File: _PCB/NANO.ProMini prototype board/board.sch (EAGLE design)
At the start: 32 parts, among them T1_5MM 5mm, T2_5MM 5mm, T3_5MM 5mm

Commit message: fixed issues - working version
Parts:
- added PROMINI_HEADER: (no value), pinhead_v2:PINHD-1X6/OCT
- added RA-02: LORA-RA-02-433MHZ, LikeCircuit:LORA-RA-02-433MHZ
- added VCC: (no value), SparkFun-Connectors:CONN_04LOCK_LONGPADS
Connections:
- new net N$1: RA-02.GND.1, RA-02.GND.2
- new net N$37: NANO.5.5V, PH1.23, PH1.24, VCC.3
- net 3.3V: now also VCC.2
- net 5V: now also VCC.4; no longer NANO.5.5V, PH1.23, PH1.24
- net GND: now also RAW.GNDBREAK; no longer RAW.GND
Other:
- moved on the sheet: 3.3/5, 3.3V_C, 5PIN1, 5PIN2, 5V, 5V_C, D_5PIN, D_B, ES32-433T20D, GND, GY-521, H1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

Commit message: update
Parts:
- removed 5PIN1, 5PIN2: (no value), SparkFun-Connectors:USB_MICRO-B_FEMALE-SMT
- removed D_B, J2: (no value), SparkFun-Connectors:CONN_02LOCK
- added H2, H3: MOUNT-HOLE3.0, holes:MOUNT-HOLE3.0
- added J4: (no value), SparkFun-Connectors:CONN_04LOCK
- added MICRO_1, MICRO_2: (no value), SparkFun-Connectors:USB_MICRO-B_SMT
- added MINI_1: USB_MINI-B_SMT, SparkFun-Connectors:USB_MINI-B_SMT
- added PIEZO_: F/CM12P, buzzer:F/CM12P
- added SW1: (no value), special:SW_DIP-4
- added U$1: USB-SERIAL-CP2102, diy-modules:USB-SERIAL-CP2102
- 3.3V, 5V, GND: device pinhead:PINHD-1X4 -> SparkFun-Connectors:CONN_05LOCK_LONGPADS
- PIEZO: value F/CM12P -> (none); device buzzer:F/CM12P -> SparkFun-Connectors:CONN_02LOCK
- VIN: device pinhead:PINHD-1X4 -> SparkFun-Connectors:CONN_04LOCK_LONGPADS
- renumbered D_5PIN to USB_DATA, VCC to BOARD_POWER
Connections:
- removed net N$36: D_B.2, USB_B.D+
- removed net N$37: BOARD_POWER.3, NANO.5.5V, PH1.23, PH1.24
- new net N$38: BOARD_POWER.3, NANO.5.5V, PH1.23, PH1.24, SW1.5, SW1.6, SW1.7, SW1.8
- new net N$39: J4.1, SW1.4
- new net N$40: J4.2, SW1.3
- new net N$41: J4.3, SW1.2
- new net N$42: J4.4, SW1.1
- net 3.3V: now also 3.3V.5, RA-02.3.3V; no longer 3.3V.1
- net 5V: now also 5V.5, MICRO_1.VBUS, MICRO_2.VBUS, MINI_1.VBUS; no longer 5PIN1.VBUS, 5PIN2.VBUS
- net D+_5PIN: now also MICRO_1.D+, MICRO_2.D+, MINI_1.D+, USB_B.D+; no longer 5PIN1.D+, 5PIN2.D+
- net D-_5PIN: now also MICRO_1.D-, MICRO_2.D-, MINI_1.D-, USB_B.D-; no longer 5PIN1.D-, 5PIN2.D-
- net GND: now also MICRO_1.GND, MICRO_2.GND, MINI_1.GND, PIEZO_.2; no longer 5PIN1.GND, 5PIN2.GND, GND.1, GND.2, GND.3, GND.4, PIEZO.2
- net N$1: now also RA-02.GND.3, RA-02.GND.4
- net N$34: now also PIEZO.2, PIEZO_.1; no longer J2.1, J2.2
- net N$35: now also GND.1, GND.2, GND.3, GND.4, GND.5; no longer D_B.1, USB_B.D-
- net SHIELD_IN: now also MICRO_1.SHIELD, MICRO_2.SHIELD, MINI_1.SHIELD; no longer 5PIN1.SHIELD, 5PIN2.SHIELD
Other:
- moved on the sheet: H1

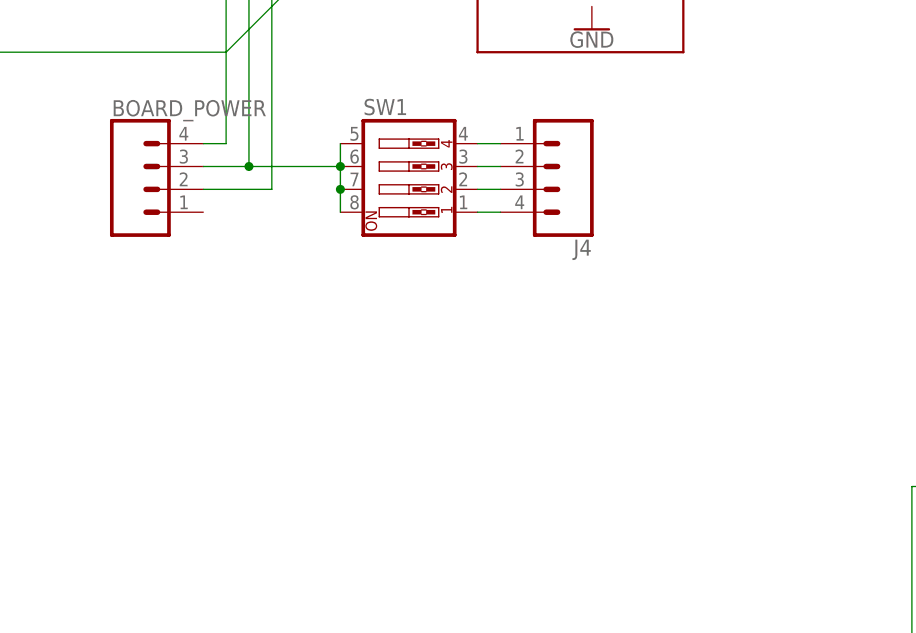
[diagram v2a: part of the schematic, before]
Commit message: board updates, LoRa
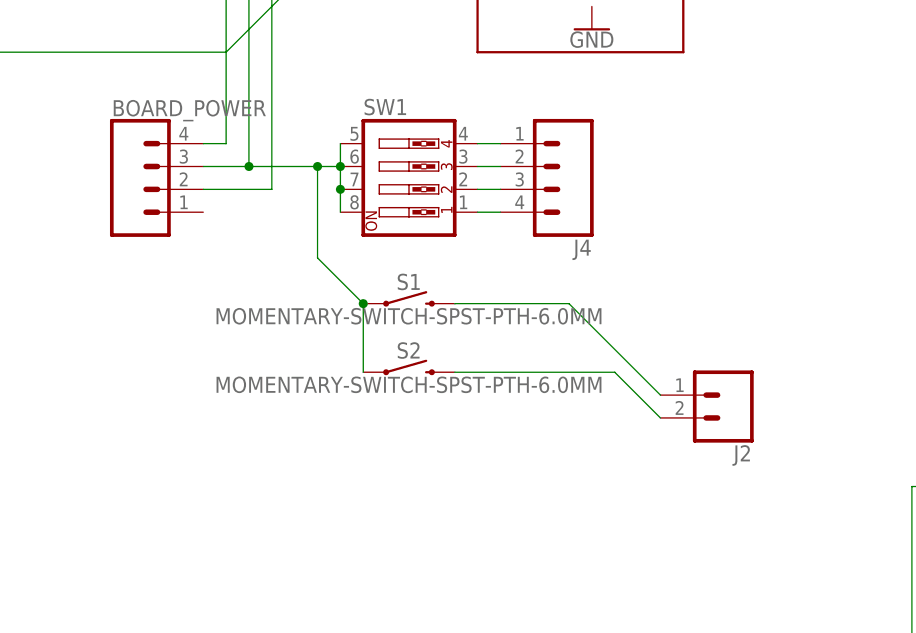
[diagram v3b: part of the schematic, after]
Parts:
- added J2: (no value), SparkFun-Connectors:CONN_02LOCK_LONGPADS
- added S1, S2: MOMENTARY-SWITCH-SPST-PTH-6.0MM, SparkFun-Switches:MOMENTARY-SWITCH-SPST-PTH-6.0MM
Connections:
- removed net N$38: BOARD_POWER.3, NANO.5.5V, PH1.23, PH1.24, SW1.5, SW1.6, SW1.7, SW1.8
- new net N$36: BOARD_POWER.3, NANO.5.5V, PH1.23, PH1.24, S1.1, S2.1, SW1.5, SW1.6, SW1.7, SW1.8
- new net N$37: J2.1, S1.2
- new net N$43: J2.2, S2.2
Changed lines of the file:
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@@
 <part name="GND" library="SparkFun-Connectors" library_urn="urn:adsk.eagle:library:513" deviceset="CONN_05" device="LOCK_LONGPADS" package3d_urn="urn:adsk.eagle:package:38107/1"/>
 <part name="VIN" library="SparkFun-Connectors" library_urn="urn:adsk.eagle:library:513" deviceset="CONN_04" device="LOCK_LONGPADS" package3d_urn="urn:adsk.eagle:package:38091/1"/>
+<part name="S1" library="SparkFun-Switches" library_urn="urn:adsk.eagle:library:535" deviceset="MOMENTARY-SWITCH-SPST" device="-PTH-6.0MM" package3d_urn="urn:adsk.eagle:package:40163/1"/>
+<part name="S2" library="SparkFun-Switches" library_urn="urn:adsk.eagle:library:535" deviceset="MOMENTARY-SWITCH-SPST" device="-PTH-6.0MM" package3d_urn="urn:adsk.eagle:package:40163/1"/>
+<part name="J2" library="SparkFun-Connectors" library_urn="urn:adsk.eagle:library:513" deviceset="CONN_02" device="LOCK_LONGPADS" package3d_urn="urn:adsk.eagle:package:38047/1"/>
 </parts>
 <sheets>
@@
 <instance part="GND" gate="G$1" x="-162.56" y="-33.02"/>
 <instance part="VIN" gate="G$1" x="-160.02" y="-53.34"/>
+<instance part="S1" gate="G$1" x="-17.78" y="-53.34"/>
+<instance part="S2" gate="G$1" x="-17.78" y="-60.96"/>
+<instance part="J2" gate="G$1" x="17.78" y="-63.5" rot="R180"/>
 </instances>
 <busses>
@@
 </segment>
 </net>
-<net name="N$38" class="0">
-<segment>
+<net name="N$39" class="0">
+<segment>
+<pinref part="SW1" gate="A" pin="4"/>
+<pinref part="J4" gate="G$1" pin="1"/>
+<wire x1="-7.62" y1="-35.56" x2="-10.16" y2="-35.56" width="0.1524" layer="91"/>
+</segment>
+</net>
+<net name="N$40" class="0">
+<segment>
+<pinref part="SW1" gate="A" pin="3"/>
+<pinref part="J4" gate="G$1" pin="2"/>
+<wire x1="-7.62" y1="-38.1" x2="-10.16" y2="-38.1" width="0.1524" layer="91"/>
+</segment>
+</net>
+<net name="N$41" class="0">
+<segment>
+<pinref part="SW1" gate="A" pin="2"/>
+<pinref part="J4" gate="G$1" pin="3"/>
+<wire x1="-7.62" y1="-40.64" x2="-10.16" y2="-40.64" width="0.1524" layer="91"/>
+</segment>
+</net>
+<net name="N$42" class="0">
+<segment>
+<pinref part="SW1" gate="A" pin="1"/>
+<pinref part="J4" gate="G$1" pin="4"/>
+<wire x1="-7.62" y1="-43.18" x2="-10.16" y2="-43.18" width="0.1524" layer="91"/>
+</segment>
+</net>
+<net name="N$35" class="0">
+<segment>
+<pinref part="GND" gate="G$1" pin="5"/>
+<pinref part="GND" gate="G$1" pin="4"/>
+<wire x1="-154.94" y1="-27.94" x2="-154.94" y2="-30.48" width="0.1524" layer="91"/>
+<pinref part="GND" gate="G$1" pin="3"/>
+<wire x1="-154.94" y1="-30.48" x2="-154.94" y2="-33.02" width="0.1524" layer="91"/>
+<junction x="-154.94" y="-30.48"/>
+<pinref part="GND" gate="G$1" pin="2"/>
+<wire x1="-154.94" y1="-33.02" x2="-154.94" y2="-35.56" width="0.1524" layer="91"/>
+<junction x="-154.94" y="-33.02"/>
+<pinref part="GND" gate="G$1" pin="1"/>
+<wire x1="-154.94" y1="-35.56" x2="-154.94" y2="-38.1" width="0.1524" layer="91"/>
+<junction x="-154.94" y="-35.56"/>
+</segment>
+</net>
+<net name="N$36" class="0">
+<segment>
+<pinref part="S1" gate="G$1" pin="1"/>
+<pinref part="S2" gate="G$1" pin="1"/>
+<wire x1="-22.86" y1="-53.34" x2="-22.86" y2="-60.96" width="0.1524" layer="91"/>
 <pinref part="SW1" gate="A" pin="5"/>
 <pinref part="SW1" gate="A" pin="6"/>
@@
 <wire x1="-35.56" y1="-7.62" x2="-27.94" y2="-7.62" width="0.1524" layer="91"/>
 <junction x="-27.94" y="-7.62"/>
-<wire x1="-25.4" y1="-38.1" x2="-35.56" y2="-38.1" width="0.1524" layer="91"/>
+<wire x1="-25.4" y1="-38.1" x2="-27.94" y2="-38.1" width="0.1524" layer="91"/>
 <junction x="-35.56" y="-38.1"/>
-</segment>
-</net>
-<net name="N$39" class="0">
-<segment>
-<pinref part="SW1" gate="A" pin="4"/>
-<pinref part="J4" gate="G$1" pin="1"/>
-<wire x1="-7.62" y1="-35.56" x2="-10.16" y2="-35.56" width="0.1524" layer="91"/>
-</segment>
-</net>
-<net name="N$40" class="0">
-<segment>
-<pinref part="SW1" gate="A" pin="3"/>
-<pinref part="J4" gate="G$1" pin="2"/>
-<wire x1="-7.62" y1="-38.1" x2="-10.16" y2="-38.1" width="0.1524" layer="91"/>
-</segment>
-</net>
-<net name="N$41" class="0">
-<segment>
-<pinref part="SW1" gate="A" pin="2"/>
-<pinref part="J4" gate="G$1" pin="3"/>
-<wire x1="-7.62" y1="-40.64" x2="-10.16" y2="-40.64" width="0.1524" layer="91"/>
-</segment>
-</net>
-<net name="N$42" class="0">
-<segment>
-<pinref part="SW1" gate="A" pin="1"/>
-<pinref part="J4" gate="G$1" pin="4"/>
-<wire x1="-7.62" y1="-43.18" x2="-10.16" y2="-43.18" width="0.1524" layer="91"/>
-</segment>
-</net>
-<net name="N$35" class="0">
-<segment>
-<pinref part="GND" gate="G$1" pin="5"/>
-<pinref part="GND" gate="G$1" pin="4"/>
-<wire x1="-154.94" y1="-27.94" x2="-154.94" y2="-30.48" width="0.1524" layer="91"/>
-<pinref part="GND" gate="G$1" pin="3"/>
-<wire x1="-154.94" y1="-30.48" x2="-154.94" y2="-33.02" width="0.1524" layer="91"/>
-<junction x="-154.94" y="-30.48"/>
-<pinref part="GND" gate="G$1" pin="2"/>
-<wire x1="-154.94" y1="-33.02" x2="-154.94" y2="-35.56" width="0.1524" layer="91"/>
-<junction x="-154.94" y="-33.02"/>
-<pinref part="GND" gate="G$1" pin="1"/>
-<wire x1="-154.94" y1="-35.56" x2="-154.94" y2="-38.1" width="0.1524" layer="91"/>
-<junction x="-154.94" y="-35.56"/>
-</segment>
-</net>
+<wire x1="-27.94" y1="-38.1" x2="-35.56" y2="-38.1" width="0.1524" layer="91"/>
+<wire x1="-22.86" y1="-53.34" x2="-27.94" y2="-48.26" width="0.1524" layer="91"/>
+<wire x1="-27.94" y1="-48.26" x2="-27.94" y2="-38.1" width="0.1524" layer="91"/>
+<junction x="-22.86" y="-53.34"/>
+<junction x="-27.94" y="-38.1"/>
+</segment>
+</net>
+<net name="N$37" class="0">
+<segment>
+<pinref part="S1" gate="G$1" pin="2"/>
+<wire x1="-12.7" y1="-53.34" x2="0" y2="-53.34" width="0.1524" layer="91"/>
+<wire x1="0" y1="-53.34" x2="10.16" y2="-63.5" width="0.1524" layer="91"/>
+<pinref part="J2" gate="G$1" pin="1"/>
+</segment>
+</net>
+<net name="N$43" class="0">
+<segment>
+<pinref part="S2" gate="G$1" pin="2"/>
+<wire x1="-12.7" y1="-60.96" x2="5.08" y2="-60.96" width="0.1524" layer="91"/>
+<wire x1="5.08" y1="-60.96" x2="10.16" y2="-66.04" width="0.1524" layer="91"/>
+<pinref part="J2" gate="G$1" pin="2"/>
+</segment>
+</net>

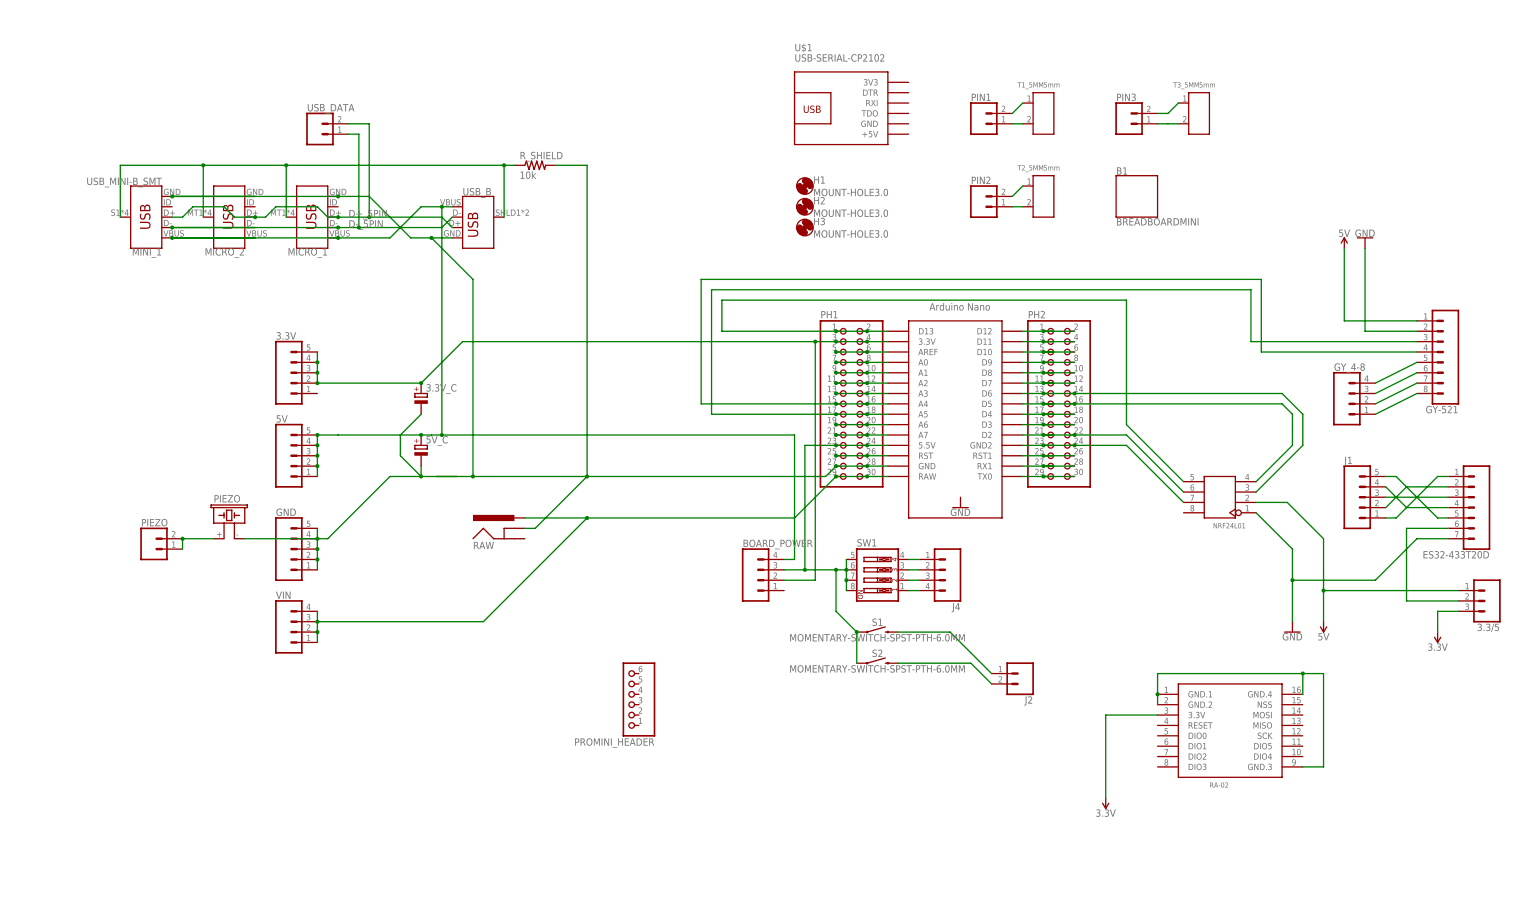
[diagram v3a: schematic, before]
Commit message: prototype PCB, air mouse example code
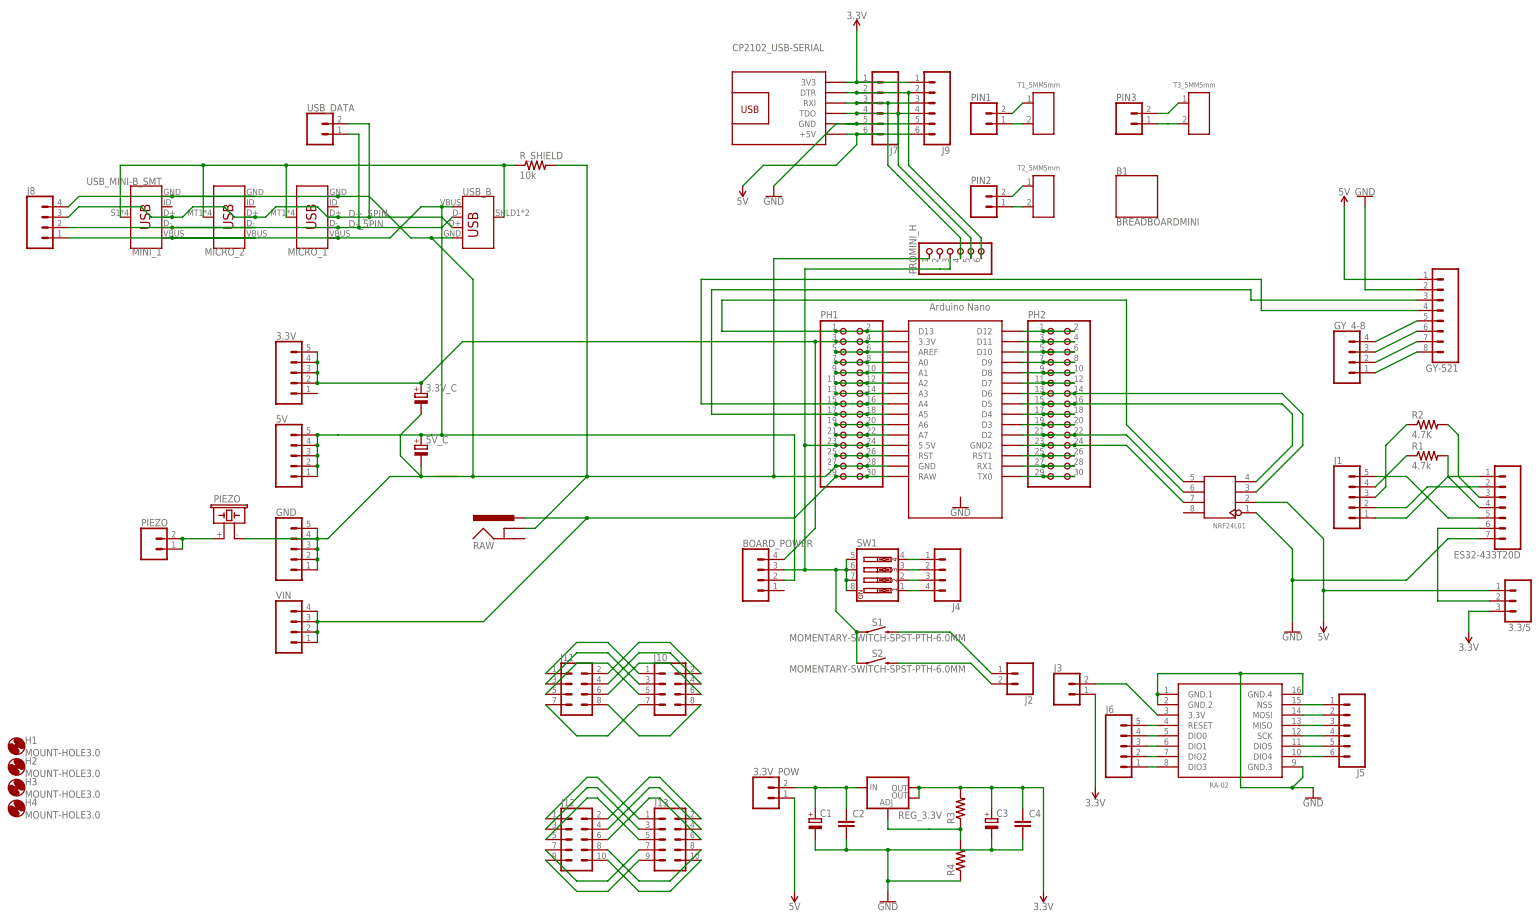
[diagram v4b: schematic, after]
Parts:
- removed PROMINI_HEADER: (no value), pinhead_v2:PINHD-1X6/OCT
- removed U$1: USB-SERIAL-CP2102, diy-modules:USB-SERIAL-CP2102
- added 3.3V_POW, J3: (no value), SparkFun-Connectors:CONN_02LOCK_LONGPADS
- added C1, C3: (no value), rcl:CPOL-EUE2.5-5
- added C2, C4: (no value), rcl:C-EU025-030X050
- added CP2102_USB-SERIAL: USB-SERIAL-CP2102, diy-modules:USB-SERIAL-CP2102
- added H4: MOUNT-HOLE3.0, holes:MOUNT-HOLE3.0
- added J10, J11: (no value), SparkFun-Connectors:CONN_04X2
- added J12, J13: (no value), SparkFun-Connectors:CONN_05X2PTH
- added J5, J7, J9: (no value), SparkFun-Connectors:CONN_06LOCK
- added J6: (no value), SparkFun-Connectors:CONN_05LOCK
- added J8: (no value), SparkFun-Connectors:CONN_04LOCK
- added PROMINI_H: (no value), pinhead_v2:PINHD-1X6/OCT
- added R1: 4.7k, rcl:R-US_0207/7
- added R2: 4.7K, rcl:R-US_0207/7
- added R3, R4: (no value), rcl:R-US_0207/7
- added REG_3.3V: (no value), SparkFun-IC-Power:V_REG_LM1117SOT223
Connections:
- removed net N$1 (its old number): RA-02.GND.1, RA-02.GND.2, RA-02.GND.3, RA-02.GND.4
- new net N$15: ES32-433T20D.4, R1.2
- new net N$38: ES32-433T20D.3, R2.2
- new net N$44: J6.1, RA-02.DIO3
- new net N$45: J6.2, RA-02.DIO2
- new net N$46: J6.3, RA-02.DIO1
- new net N$47: J6.4, RA-02.DIO0
- new net N$48: J6.5, RA-02.RESET
- new net N$49: J5.1, RA-02.NSS
- new net N$50: J5.2, RA-02.MOSI
- new net N$51: J5.3, RA-02.MISO
- new net N$52: J5.4, RA-02.SCK
- new net N$53: J5.5, RA-02.DIO5
- new net N$54: J5.6, RA-02.DIO4
- new net N$55: J10.1, J11.1
- new net N$56: CP2102_USB-SERIAL.DTR, J7.2, J9.2, PROMINI_H.6
- new net N$57: CP2102_USB-SERIAL.RXI, J7.3, J9.3, PROMINI_H.4
- new net N$58: J10.3, J11.3
- new net N$59: J10.5, J11.5
- new net N$60: J10.7, J11.7
- new net N$61: J10.2, J11.2
- new net N$62: CP2102_USB-SERIAL.TDO, J7.4, J9.4, PROMINI_H.5
- new net N$63: J10.4, J11.4
- new net N$64: J10.6, J11.6
- new net N$65: J10.8, J11.8
- new net N$66: J12.1, J13.1
- new net N$67: J12.3, J13.3
- new net N$68: J12.5, J13.5
- new net N$69: J12.9, J13.9
- new net N$70: J12.7, J13.7
- new net N$71: J12.2, J13.2
- new net N$72: J12.4, J13.4
- new net N$73: J12.6, J13.6
- new net N$74: J12.10, J13.10
- new net N$75: J12.8, J13.8
- new net N$76: J3.2, RA-02.3.3V
- new net N$77: 3.3V_POW.2, C1.+, C2.1, REG_3.3V.IN
- new net N$79: R3.1, R4.2, REG_3.3V.ADJ
- net 3.3V: now also BOARD_POWER.4, C3.+, C4.1, CP2102_USB-SERIAL.3V3, J3.1, J7.1, J9.1, R3.2, REG_3.3V.OUT, REG_3.3V.OUT@1; no longer BOARD_POWER.2, RA-02.3.3V
- net 5V: now also 3.3V_POW.1, BOARD_POWER.2, CP2102_USB-SERIAL.+5V, J7.6, J8.1, J9.6; no longer BOARD_POWER.4
- net D+_5PIN: now also J8.3
- net D-_5PIN: now also J8.2
- net GND: now also C1.-, C2.2, C3.-, C4.2, CP2102_USB-SERIAL.GND, J7.5, J8.4, J9.5, PROMINI_H.1, R4.1, RA-02.GND.1, RA-02.GND.2, RA-02.GND.3, RA-02.GND.4
- net N$13: now also R1.1; no longer ES32-433T20D.4
- net N$14: now also R2.1; no longer ES32-433T20D.3
- net N$36: now also PROMINI_H.3
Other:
- moved on the sheet: 3.3/5, ES32-433T20D, GY-521, GY_4-8, H1, H2, H3, J1
